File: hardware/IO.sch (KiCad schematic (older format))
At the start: 14 parts, among them J3 Input, J4 Output, SW2 Interrupt, SW3 Port B

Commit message: Working on layout
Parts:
- removed J3: Input, Connector_PinHeader_2.54mm:PinHeader_2x06_P2.54mm_Vertical, symbol Connector_Generic:Conn_02x06_Odd_Even
- removed J4: Output, Connector_PinHeader_2.54mm:PinHeader_2x06_P2.54mm_Vertical, symbol Connector_Generic:Conn_02x06_Odd_Even
- added C17: 100nF, Capacitor_THT:C_Rect_L4.0mm_W2.5mm_P2.50mm, symbol Device:C
- added R9: 10k, Resistor_THT:R_Axial_DIN0207_L6.3mm_D2.5mm_P7.62mm_Horizontal, symbol Device:R
- added SW4: ~NMI, Button_Switch_THT:SW_PUSH_6mm_H4.3mm, symbol Switch:SW_Push
- D0: value LED -> LED0
- D1: value LED -> LED1
- D2: value LED -> LED2
- D3: value LED -> LED3
- D4: value LED -> LED4
- D5: value LED -> LED5
- D6: value LED -> LED6
- D7: value LED -> LED7
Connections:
- net labels removed: ACIAReady, BE, RDY, SYNC, VPB, ~IRQ
- wire segments 111 -> 84
- no-connect marks 3 -> 0
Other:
- moved on the sheet: D0, D1, D2, D3, D4, D5, D6, D7, RN1, RN2, SW2, SW3

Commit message: Working on layout
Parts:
- added J3: Conn_02x20_Odd_Even, Connector_PinHeader_2.54mm:PinHeader_2x20_P2.54mm_Horizontal, symbol Connector_Generic:Conn_02x20_Odd_Even
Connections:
- net +5V: now also J3.40 (Pin_40)
- net GND: now also J3.39 (Pin_39)
- new net 1MHz: J3.20 (Pin_20)
- new net A0: J3.1 (Pin_1)
- new net A1: J3.3 (Pin_3)
- new net A10: J3.21 (Pin_21)
- new net A11: J3.23 (Pin_23)
- new net A12: J3.25 (Pin_25)
- new net A13: J3.27 (Pin_27)
- new net A14: J3.29 (Pin_29)
- new net A15: J3.31 (Pin_31)
- new net A2: J3.5 (Pin_5)
- new net A3: J3.7 (Pin_7)
- new net A4: J3.9 (Pin_9)
- new net A5: J3.11 (Pin_11)
- new net A6: J3.13 (Pin_13)
- new net A7: J3.15 (Pin_15)
- new net A8: J3.17 (Pin_17)
- new net A9: J3.19 (Pin_19)
- new net D0: J3.2 (Pin_2)
- new net D1: J3.4 (Pin_4)
- new net D2: J3.6 (Pin_6)
- new net D3: J3.8 (Pin_8)
- new net D4: J3.10 (Pin_10)
- new net D5: J3.12 (Pin_12)
- new net D6: J3.14 (Pin_14)
- new net D7: J3.16 (Pin_16)
- new net R~W: J3.18 (Pin_18)
- new net ~RESET: J3.22 (Pin_22)
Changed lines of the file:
@@
 $Descr A4 11693 8268
 encoding utf-8
-Sheet 5 6
+Sheet 4 6
 Title "Retro PC"
 Date "2019-10-08"
@@
 Text HLabel 1600 6400 2    50   Output ~ 0
 ~NMI
+Text HLabel 10350 2150 2    50   Input ~ 0
+R~W
+Text HLabel 8800 1150 0    50   Input ~ 0
+A[15..0]
+Text HLabel 8800 1050 0    50   BiDi ~ 0
+D[7..0]
+Entry Wire Line
+	9250 1550 9350 1450
+Entry Wire Line
+	9250 1450 9350 1350
+Entry Wire Line
+	9250 1650 9350 1550
+Entry Wire Line
+	9250 1750 9350 1650
+Entry Wire Line
+	9250 1850 9350 1750
+Entry Wire Line
+	9250 1950 9350 1850
+Entry Wire Line
+	9250 2050 9350 1950
+Entry Wire Line
+	9250 2150 9350 2050
+Entry Wire Line
+	9250 2250 9350 2150
+Entry Wire Line
+	9250 2350 9350 2250
+Entry Wire Line
+	9350 2350 9250 2450
+Entry Wire Line
+	9250 2550 9350 2450
+Entry Wire Line
+	9250 2850 9350 2750
+Entry Wire Line
+	9350 2550 9250 2650
+Entry Wire Line
+	9250 2750 9350 2650
+Entry Wire Line
+	9250 2950 9350 2850
+Entry Wire Line
+	10700 1450 10600 1350
+Entry Wire Line
+	10700 1550 10600 1450
+Entry Wire Line
+	10700 1650 10600 1550
+Entry Wire Line
+	10700 1750 10600 1650
+Entry Wire Line
+	10700 1850 10600 1750
+Entry Wire Line
+	10700 1950 10600 1850
+Entry Wire Line
+	10700 2050 10600 1950
+Entry Wire Line
+	10700 2150 10600 2050
+Wire Wire Line
+	9350 1350 9750 1350
+Wire Wire Line
+	9350 1450 9750 1450
+Wire Wire Line
+	9350 1550 9750 1550
+Wire Wire Line
+	9350 1650 9750 1650
+Wire Wire Line
+	9350 1950 9750 1950
+Wire Wire Line
+	9350 2050 9750 2050
+Wire Wire Line
+	9350 2150 9750 2150
+Wire Wire Line
+	9350 2250 9750 2250
+Wire Wire Line
+	9350 2350 9750 2350
+Wire Wire Line
+	9350 2450 9750 2450
+Wire Wire Line
+	9350 2550 9750 2550
+Wire Wire Line
+	9350 2650 9750 2650
+Wire Wire Line
+	9350 2850 9750 2850
+Wire Wire Line
+	9350 2750 9750 2750
+Wire Wire Line
+	9350 1750 9750 1750
+Wire Wire Line
+	9350 1850 9750 1850
+Text Label 9450 1350 0    50   ~ 0
+A0
+Text Label 9450 1550 0    50   ~ 0
+A2
+Text Label 9450 1650 0    50   ~ 0
+A3
+Text Label 9450 1750 0    50   ~ 0
+A4
+Text Label 9450 1850 0    50   ~ 0
+A5
+Text Label 9450 1950 0    50   ~ 0
+A6
+Text Label 9450 2050 0    50   ~ 0
+A7
+Text Label 9450 2150 0    50   ~ 0
+A8
+Text Label 9450 2250 0    50   ~ 0
+A9
+Text Label 9450 2350 0    50   ~ 0
+A10
+Text Label 9450 2450 0    50   ~ 0
+A11
+Text Label 9450 2550 0    50   ~ 0
+A12
+Text Label 9450 2650 0    50   ~ 0
+A13
+Text Label 9450 2750 0    50   ~ 0
+A14
+Text Label 9450 2850 0    50   ~ 0
+A15
+Wire Wire Line
+	10250 1350 10600 1350
+Wire Wire Line
+	10250 1450 10600 1450
+Wire Wire Line
+	10250 1550 10600 1550
+Wire Wire Line
+	10250 1650 10600 1650
+Wire Wire Line
+	10250 1750 10600 1750
+Wire Wire Line
+	10250 1850 10600 1850
+Wire Wire Line
+	10250 1950 10600 1950
+Wire Wire Line
+	10250 2050 10600 2050
+Text Label 10400 1350 0    50   ~ 0
+D0
+Text Label 10400 1450 0    50   ~ 0
+D1
+Text Label 10400 1550 0    50   ~ 0
+D2
+Text Label 10400 1650 0    50   ~ 0
+D3
+Text Label 10400 1750 0    50   ~ 0
+D4
+Text Label 10400 1850 0    50   ~ 0
+D5
+Text Label 10400 1950 0    50   ~ 0
+D6
+Text Label 10400 2050 0    50   ~ 0
+D7
+$Comp
+L Connector_Generic:Conn_02x20_Odd_Even J3
+U 1 1 5DBDED7E
+P 9950 2250
+F 0 "J3" H 10000 3367 50  0000 C CNN
+F 1 "Conn_02x20_Odd_Even" H 10000 3276 50  0000 C CNN
+F 2 "Connector_PinHeader_2.54mm:PinHeader_2x20_P2.54mm_Horizontal" H 9950 2250 50  0001 C CNN
+F 3 "https://cdn.harwin.com/pdfs/M20-974.pdf" H 9950 2250 50  0001 C CNN
+F 4 "Harwin" H 9950 2250 50  0001 C CNN "Mfr."
+F 5 "M20-9742046" H 9950 2250 50  0001 C CNN "Mfr. No."
+F 6 "855-M20-9742046" H 9950 2250 50  0001 C CNN "Mouser"
+	1    9950 2250
+	1    0    0    -1
+$EndComp
+Wire Bus Line
+	9250 1150 8800 1150
+Wire Bus Line
+	8800 1050 10700 1050
+Wire Wire Line
+	10350 2150 10250 2150
+$Comp
+L power:GND #PWR?
+U 1 1 5DC0914B
+P 9650 3600
+AR Path="/5DC0914B" Ref="#PWR?"  Part="1"
+AR Path="/5EB09E21/5DC0914B" Ref="#PWR?"  Part="1"
+AR Path="/5EC67F7B/5DC0914B" Ref="#PWR070"  Part="1"
+F 0 "#PWR070" H 9650 3350 50  0001 C CNN
+F 1 "GND" H 9655 3427 50  0000 C CNN
+F 2 "" H 9650 3600 50  0001 C CNN
+F 3 "" H 9650 3600 50  0001 C CNN
+	1    9650 3600
+	1    0    0    -1
+$EndComp
+Wire Wire Line
+	9650 3600 9650 3250
+Wire Wire Line
+	9750 3250 9650 3250
+$Comp
+L power:+5V #PWR?
+U 1 1 5DC11208
+P 10650 3150
+AR Path="/5DC11208" Ref="#PWR?"  Part="1"
+AR Path="/5EB09E21/5DC11208" Ref="#PWR?"  Part="1"
+AR Path="/5EC67F7B/5DC11208" Ref="#PWR071"  Part="1"
+F 0 "#PWR071" H 10650 3000 50  0001 C CNN
+F 1 "+5V" H 10665 3323 50  0000 C CNN
+F 2 "" H 10650 3150 50  0001 C CNN
+F 3 "" H 10650 3150 50  0001 C CNN
+	1    10650 3150
+	1    0    0    -1
+$EndComp
+Wire Wire Line
+	10650 3150 10650 3250
+Wire Wire Line
+	10250 3250 10650 3250
+Text Label 9450 1450 0    50   ~ 0
+A1
+Text HLabel 10350 2250 2    50   Input ~ 0
+1MHz
+Wire Wire Line
+	10350 2250 10250 2250
+Text HLabel 10350 2350 2    50   Output ~ 0
+~RESET
+Wire Wire Line
+	10350 2350 10250 2350
 Wire Bus Line
 	2850 3450 2850 4150
 Wire Bus Line
 	1800 1000 1800 1700
+Wire Bus Line
+	10700 1050 10700 2150
+Wire Bus Line
+	9250 1150 9250 2950
 $EndSCHEMATC

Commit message: Working on layout
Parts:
- X3: renamed from J3; value Conn_02x20_Odd_Even -> Expansion
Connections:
- net ~IRQ: now reaches X3.24 (Pin_24)
- net 1MHz renamed Clock
- no-connect marks 0 -> 10
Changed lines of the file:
@@
 $Descr A4 11693 8268
 encoding utf-8
-Sheet 4 6
+Sheet 3 6
 Title "Retro PC"
 Date "2019-10-08"
@@
 D7
 $Comp
-L Connector_Generic:Conn_02x20_Odd_Even J3
+L Connector_Generic:Conn_02x20_Odd_Even X3
 U 1 1 5DBDED7E
 P 9950 2250
-F 0 "J3" H 10000 3367 50  0000 C CNN
-F 1 "Conn_02x20_Odd_Even" H 10000 3276 50  0000 C CNN
+F 0 "X3" H 10000 3367 50  0000 C CNN
+F 1 "Expansion" H 10000 3276 50  0000 C CNN
 F 2 "Connector_PinHeader_2.54mm:PinHeader_2x20_P2.54mm_Horizontal" H 9950 2250 50  0001 C CNN
 F 3 "https://cdn.harwin.com/pdfs/M20-974.pdf" H 9950 2250 50  0001 C CNN
@@
 A1
 Text HLabel 10350 2250 2    50   Input ~ 0
-1MHz
+Clock
 Wire Wire Line
 	10350 2250 10250 2250
@@
 Wire Wire Line
 	10350 2350 10250 2350
+Text HLabel 10350 2450 2    50   Input ~ 0
+~IRQ
+Wire Wire Line
+	10350 2450 10250 2450
+NoConn ~ 9750 3150
+NoConn ~ 9750 3050
+NoConn ~ 9750 2950
+NoConn ~ 10250 3150
+NoConn ~ 10250 3050
+NoConn ~ 10250 2950
+NoConn ~ 10250 2850
+NoConn ~ 10250 2750
+NoConn ~ 10250 2650
+NoConn ~ 10250 2550
 Wire Bus Line
 	2850 3450 2850 4150

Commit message: First version of the layout
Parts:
- R9: Mfr. Vishay / BC Components -> Yageo; Mfr. No. SFR25H0001002JR500 -> MFP-25BRD52-10K; Mouser 594-SFR25H0001002JR5 -> 603-MFP-25BRD52-10K
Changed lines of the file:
@@
 F 1 "10k" H 920 6005 50  0000 L CNN
 F 2 "Resistor_THT:R_Axial_DIN0207_L6.3mm_D2.5mm_P7.62mm_Horizontal" V 780 6050 50  0001 C CNN
-F 3 "https://www.mouser.de/datasheet/2/427/sfr16s25-239894.pdf" H 850 6050 50  0001 C CNN
-F 4 "Vishay / BC Components" H 850 6050 50  0001 C CNN "Mfr."
-F 5 "SFR25H0001002JR500" H 850 6050 50  0001 C CNN "Mfr. No."
-F 6 "594-SFR25H0001002JR5" H 850 6050 50  0001 C CNN "Mouser"
+F 3 "https://www.mouser.de/datasheet/2/447/Yageo%20LR_MFP_2013-594635.pdf" H 850 6050 50  0001 C CNN
+F 4 "Yageo" H 850 6050 50  0001 C CNN "Mfr."
+F 5 "MFP-25BRD52-10K" H 850 6050 50  0001 C CNN "Mfr. No."
+F 6 "603-MFP-25BRD52-10K" H 850 6050 50  0001 C CNN "Mouser"
 	1    850  6050
 	1    0    0    -1

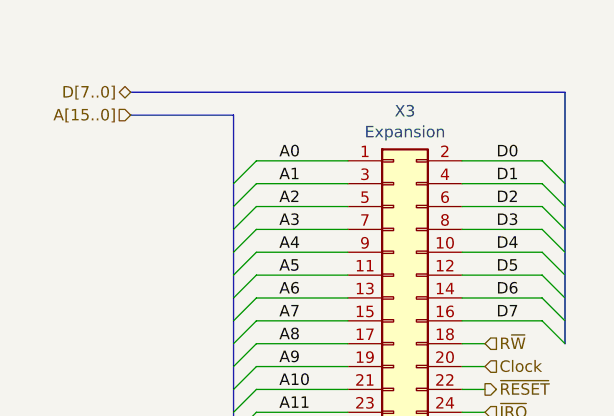
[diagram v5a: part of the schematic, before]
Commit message: Replace LCD
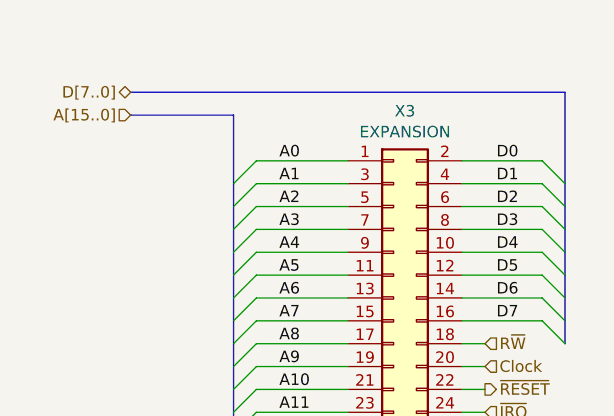
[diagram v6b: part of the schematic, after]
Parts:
- X3: value Expansion -> EXPANSION
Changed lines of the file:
@@
 P 9950 2250
 F 0 "X3" H 10000 3367 50  0000 C CNN
-F 1 "Expansion" H 10000 3276 50  0000 C CNN
+F 1 "EXPANSION" H 10000 3276 50  0000 C CNN
 F 2 "Connector_PinHeader_2.54mm:PinHeader_2x20_P2.54mm_Horizontal" H 9950 2250 50  0001 C CNN
 F 3 "https://cdn.harwin.com/pdfs/M20-974.pdf" H 9950 2250 50  0001 C CNN

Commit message: Finalize schematic and layout. Add switch for carrier detect
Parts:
- added SW5: CARRIER, Button_Switch_THT:SW_E-Switch_EG1224_SPDT_Angled, symbol Switch:SW_SPDT
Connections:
- net +5V: now also SW5.1 (A)
- net GND: now also SW5.3 (C)
- net ~TerminalReady: now reaches X3.26 (Pin_26)
- new net ~CarrierDetect: SW5.2 (B)
- no-connect marks 10 -> 9
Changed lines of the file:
@@
 Date "2019-10-08"
 Rev "1.0"
-Comp ""
+Comp "https://www.kampis-elektroecke.de"
 Comment1 "Author: Daniel Kampert"
 Comment2 ""
@@
 NoConn ~ 10250 2750
 NoConn ~ 10250 2650
-NoConn ~ 10250 2550
+Text HLabel 10350 2550 2    50   Input ~ 0
+~TerminalReady
+Wire Wire Line
+	10350 2550 10250 2550
+Text HLabel 3850 6200 0    50   Output ~ 0
+~CarrierDetect
+$Comp
+L Switch:SW_SPDT SW5
+U 1 1 5DC04457
+P 4050 6200
+F 0 "SW5" H 4050 6485 50  0000 C CNN
+F 1 "CARRIER" H 4050 6394 50  0000 C CNN
+F 2 "Button_Switch_THT:SW_E-Switch_EG1224_SPDT_Angled" H 4050 6200 50  0001 C CNN
+F 3 "https://www.mouser.de/datasheet/2/140/EG-345873.pdf" H 4050 6200 50  0001 C CNN
+F 4 "E-Switch" H 4050 6200 50  0001 C CNN "Mfr."
+F 5 "EG1224" H 4050 6200 50  0001 C CNN "Mfr. No."
+F 6 "612-EG1224" H 4050 6200 50  0001 C CNN "Mouser"
+	1    4050 6200
+	1    0    0    -1
+$EndComp
+$Comp
+L power:GND #PWR?
+U 1 1 5DC0FBD8
+P 4350 6400
+AR Path="/5DC0FBD8" Ref="#PWR?"  Part="1"
+AR Path="/5EB09E21/5DC0FBD8" Ref="#PWR?"  Part="1"
+AR Path="/5EC67F7B/5DC0FBD8" Ref="#PWR048"  Part="1"
+F 0 "#PWR048" H 4350 6150 50  0001 C CNN
+F 1 "GND" H 4355 6227 50  0000 C CNN
+F 2 "" H 4350 6400 50  0001 C CNN
+F 3 "" H 4350 6400 50  0001 C CNN
+	1    4350 6400
+	1    0    0    -1
+$EndComp
+$Comp
+L power:+5V #PWR?
+U 1 1 5DC13EF2
+P 4350 6050
+AR Path="/5DC13EF2" Ref="#PWR?"  Part="1"
+AR Path="/5E9728CC/5DC13EF2" Ref="#PWR?"  Part="1"
+AR Path="/5EC67F7B/5DC13EF2" Ref="#PWR032"  Part="1"
+F 0 "#PWR032" H 4350 5900 50  0001 C CNN
+F 1 "+5V" H 4365 6223 50  0000 C CNN
+F 2 "" H 4350 6050 50  0001 C CNN
+F 3 "" H 4350 6050 50  0001 C CNN
+	1    4350 6050
+	1    0    0    -1
+$EndComp
+Wire Wire Line
+	4250 6100 4350 6100
+Wire Wire Line
+	4350 6100 4350 6050
+Wire Wire Line
+	4250 6300 4350 6300
+Wire Wire Line
+	4350 6300 4350 6400
 Wire Bus Line
 	2850 3450 2850 4150
